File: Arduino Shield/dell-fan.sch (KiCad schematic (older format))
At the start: 50 parts, among them J1 Power, P1 Digital, P10 CONN_01X01, P11 CONN_01X01, P13 CONN_01X01, P2 Power, P3 Analog, P4 Analog, P5 PWM, P6 PWM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

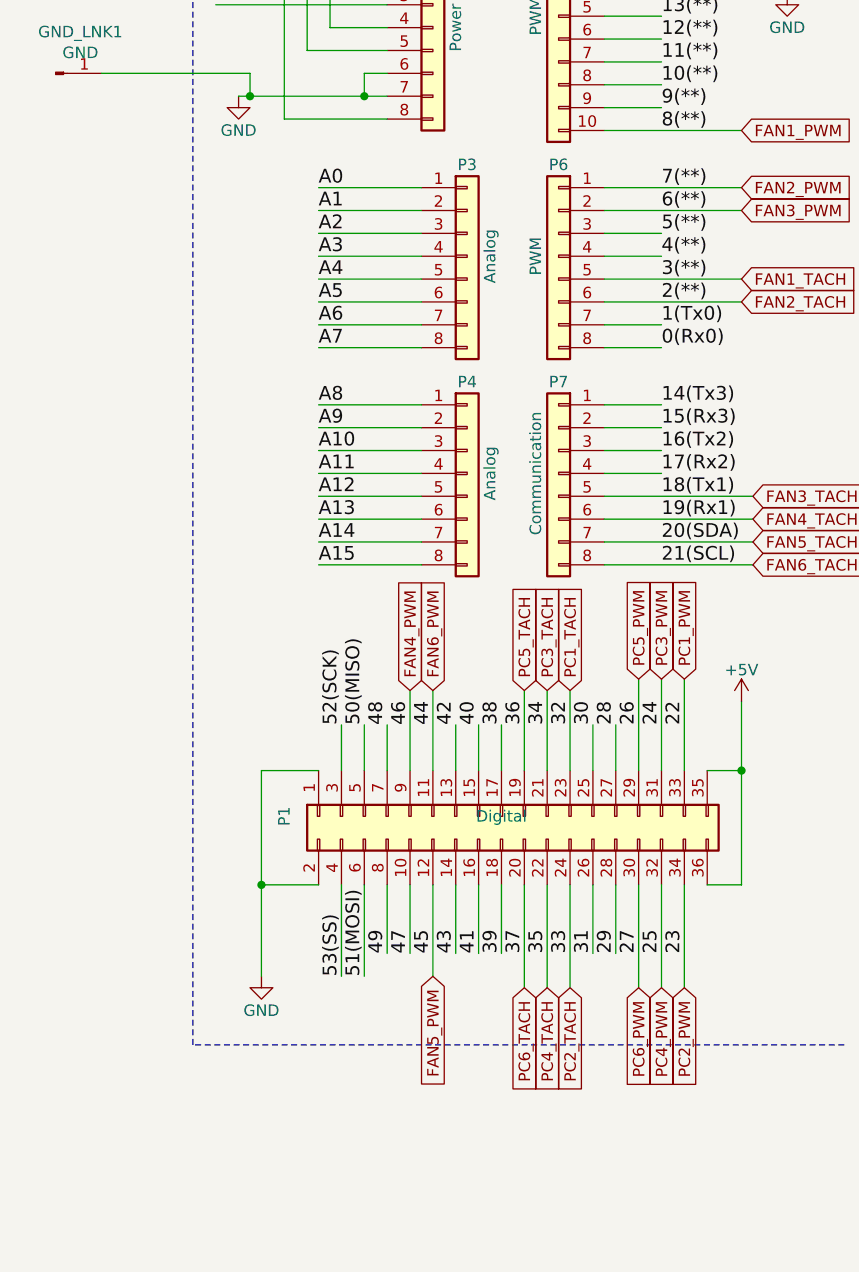
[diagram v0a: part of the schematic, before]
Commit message: moved PC Tach and PWM to D554-d69
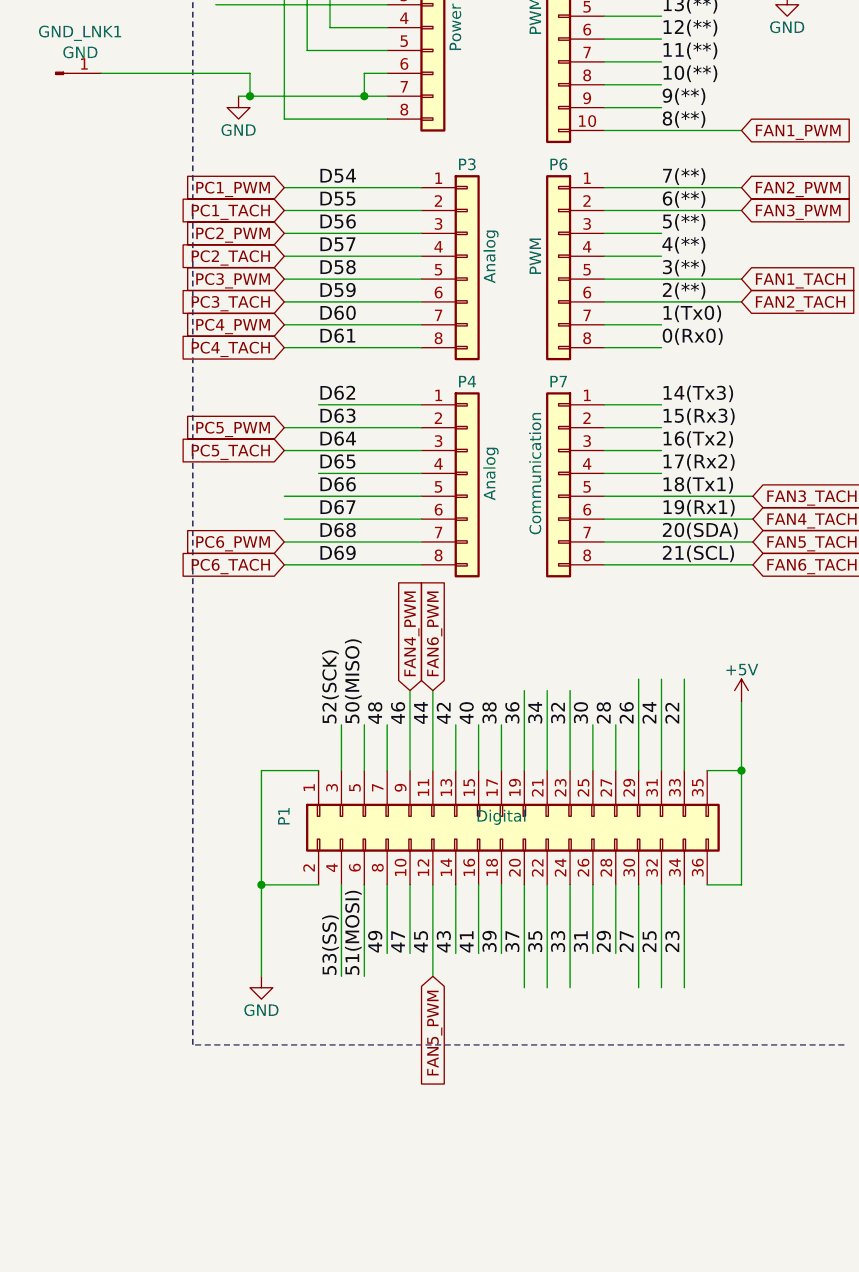
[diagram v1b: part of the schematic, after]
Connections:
- net labels added: D54, D55, D56, D57, D58, D59, D60, D61, D62, D63, D64, D65, D66, D67, D68, D69
- net labels removed: A0, A1, A10, A11, A12, A13, A14, A15, A2, A3, A4, A5, A6, A7, A8, A9
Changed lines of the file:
@@
 Vin
 Text Label 8900 2300 0    60   ~ 0
-A0
+D54
 Text Label 8900 2400 0    60   ~ 0
-A1
+D55
 Text Label 8900 2500 0    60   ~ 0
-A2
+D56
 Text Label 8900 2600 0    60   ~ 0
-A3
+D57
 Text Label 8900 2700 0    60   ~ 0
-A4
+D58
 Text Label 8900 2900 0    60   ~ 0
-A6
+D60
 Text Label 8900 3000 0    60   ~ 0
-A7
+D61
 Text Label 8900 3250 0    60   ~ 0
-A8
+D62
 Text Label 8900 3350 0    60   ~ 0
-A9
+D63
 Text Label 8900 3450 0    60   ~ 0
-A10
+D64
 Text Label 8900 3550 0    60   ~ 0
-A11
+D65
 Text Label 8900 3650 0    60   ~ 0
-A12
+D66
 Text Label 8900 3750 0    60   ~ 0
-A13
+D67
 Text Label 8900 3850 0    60   ~ 0
-A14
+D68
 Text Label 8900 3950 0    60   ~ 0
-A15
+D69
 Text Label 10500 4650 1    60   ~ 0
 22
@@
 	9350 3250 8900 3250
 Wire Wire Line
-	8900 3350 9350 3350
-Wire Wire Line
-	9350 3450 8900 3450
-Wire Wire Line
 	8900 3550 9350 3550
-Wire Wire Line
-	9350 3650 8900 3650
-Wire Wire Line
-	8900 3750 9350 3750
-Wire Wire Line
-	9350 3850 8900 3850
-Wire Wire Line
-	8900 3950 9350 3950
 Wire Wire Line
 	10400 3250 10150 3250
@@
 	1900 4550 1900 5000
 Connection ~ 1900 5000
-Wire Wire Line
-	8900 3000 9350 3000
-Wire Wire Line
-	9350 2900 8900 2900
-Wire Wire Line
-	9350 2700 8900 2700
-Wire Wire Line
-	8900 2600 9350 2600
-Wire Wire Line
-	9350 2500 8900 2500
-Wire Wire Line
-	8900 2400 9350 2400
-Wire Wire Line
-	9350 2300 8900 2300
 $Comp
 L Connector_Generic:Conn_01x08 P3
@@
 $EndComp
 Text Label 8900 2800 0    60   ~ 0
-A5
-Wire Wire Line
-	8900 2800 9350 2800
+D59
 $Comp
 L Connector_Generic:Conn_01x08 P6
@@
 Text GLabel 1100 1200 0    50   Input ~ 0
 FAN1_12v
-Text GLabel 10500 4450 1    50   Input ~ 0
+Text GLabel 8750 2300 0    50   Input ~ 0
 PC1_PWM
 Text GLabel 1100 700  0    50   Input ~ 0
@@
 Text Label 6050 3800 0    50   ~ 0
 NC
-Text GLabel 10400 4450 1    50   Input ~ 0
+Text GLabel 8750 2700 0    50   Input ~ 0
 PC3_PWM
-Text GLabel 10300 4450 1    50   Input ~ 0
+Text GLabel 8750 3350 0    50   Input ~ 0
 PC5_PWM
-Text GLabel 10000 4500 1    50   Input ~ 0
+Text GLabel 8750 2400 0    50   Input ~ 0
 PC1_TACH
-Text GLabel 10000 5800 3    50   Input ~ 0
+Text GLabel 8750 2600 0    50   Input ~ 0
 PC2_TACH
-Text GLabel 9900 4500 1    50   Input ~ 0
+Text GLabel 8750 2800 0    50   Input ~ 0
 PC3_TACH
-Text GLabel 9900 5800 3    50   Input ~ 0
+Text GLabel 8750 3000 0    50   Input ~ 0
 PC4_TACH
-Text GLabel 9800 4500 1    50   Input ~ 0
+Text GLabel 8750 3450 0    50   Input ~ 0
 PC5_TACH
-Text GLabel 9800 5800 3    50   Input ~ 0
+Text GLabel 8750 3950 0    50   Input ~ 0
 PC6_TACH
 Text GLabel 10750 2700 2    50   Input ~ 0
@@
 Text GLabel 9400 5750 3    50   Input ~ 0
 FAN5_PWM
-Text GLabel 9400 4500 1    50   Input ~ 0
-FAN6_PWM
-Text GLabel 10750 2050 2    50   Input ~ 0
-FAN1_PWM
 $Comp
 L Device:R_US R9
@@
 Wire Wire Line
 	10500 4450 10500 4850
-Text GLabel 10300 5800 3    50   Input ~ 0
+Text GLabel 8750 3850 0    50   Input ~ 0
 PC6_PWM
-Text GLabel 10400 5800 3    50   Input ~ 0
+Text GLabel 8750 2900 0    50   Input ~ 0
 PC4_PWM
-Text GLabel 10500 5800 3    50   Input ~ 0
+Text GLabel 8750 2500 0    50   Input ~ 0
 PC2_PWM
 Wire Wire Line
@@
 Text Notes 1750 5750 0    50   ~ 0
 NC
+Text GLabel 10750 2050 2    50   Input ~ 0
+FAN1_PWM
+Wire Wire Line
+	8750 2300 9350 2300
+Wire Wire Line
+	8750 2400 9350 2400
+Wire Wire Line
+	8750 2600 9350 2600
+Wire Wire Line
+	8750 2500 9350 2500
+Wire Wire Line
+	8750 2700 9350 2700
+Wire Wire Line
+	8750 2800 9350 2800
+Wire Wire Line
+	8750 3000 9350 3000
+Wire Wire Line
+	8750 2900 9350 2900
+Text GLabel 9400 4500 1    50   Input ~ 0
+FAN6_PWM
+Wire Wire Line
+	8750 3950 9350 3950
+Wire Wire Line
+	8750 3850 9350 3850
+Wire Wire Line
+	8750 3750 9350 3750
+Wire Wire Line
+	8750 3350 9350 3350
+Wire Wire Line
+	8750 3450 9350 3450
+Wire Wire Line
+	8750 3650 9350 3650
 $EndSCHEMATC

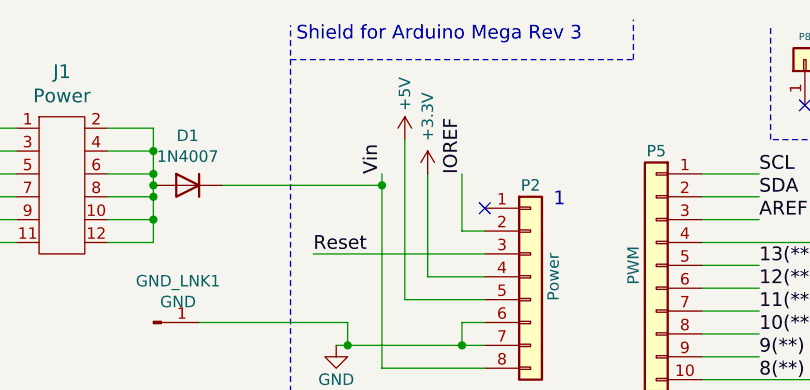
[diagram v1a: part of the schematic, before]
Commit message: fixed ground plane issue
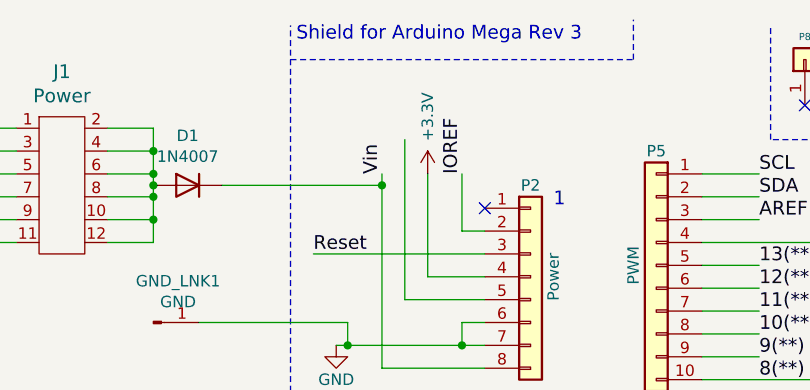
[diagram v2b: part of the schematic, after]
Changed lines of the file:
@@
 Reset
-$Comp
-L power:+5V #PWR02
-U 1 1 56D71D10
-P 8850 1000
-F 0 "#PWR02" H 8850 850 50  0001 C CNN
-F 1 "+5V" V 8850 1200 50  0000 C CNN
-F 2 "" H 8850 1000 50  0000 C CNN
-F 3 "" H 8850 1000 50  0000 C CNN
-	1    8850 1000
-	1    0    0    -1
-$EndComp
 $Comp
 L power:GND #PWR03

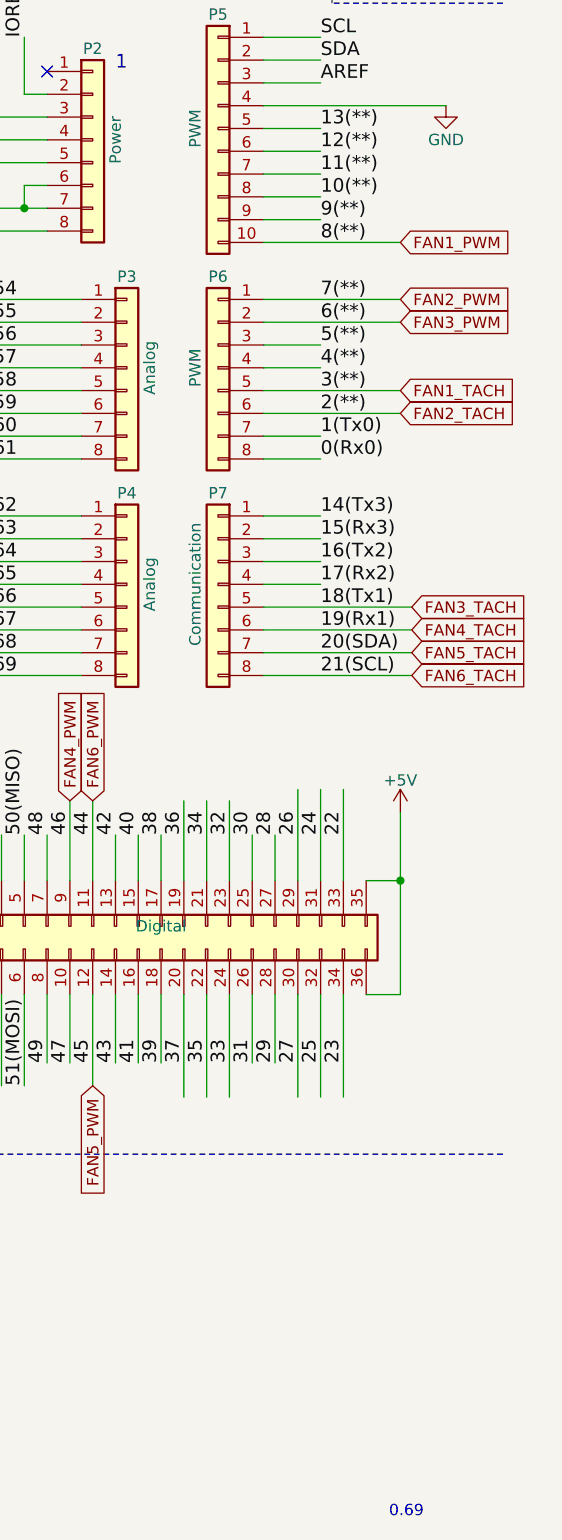
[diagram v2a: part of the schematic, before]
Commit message: No interrupts means better pin placement
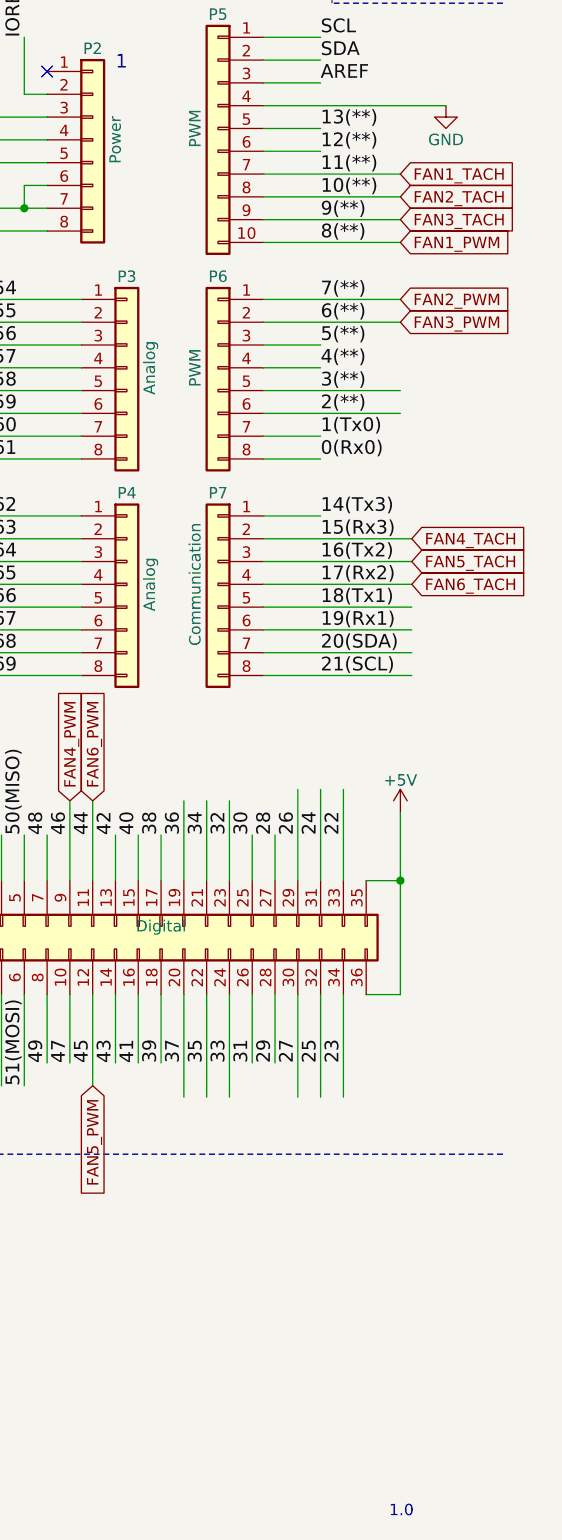
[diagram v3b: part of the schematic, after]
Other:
- note added: "1.0"
- note removed: "0.69"
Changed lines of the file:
@@
 	10400 1650 10150 1650
 Wire Wire Line
-	10150 1750 10400 1750
-Wire Wire Line
-	10150 1850 10400 1850
-Wire Wire Line
-	10400 1950 10150 1950
-Wire Wire Line
 	10400 2500 10150 2500
 Wire Wire Line
@@
 Wire Wire Line
 	10400 3250 10150 3250
-Wire Wire Line
-	10150 3350 10400 3350
-Wire Wire Line
-	10400 3450 10150 3450
-Wire Wire Line
-	10150 3550 10400 3550
 Wire Wire Line
 	10200 4850 10200 4650
@@
 Text GLabel 8750 3950 0    50   Input ~ 0
 PC6_TACH
-Text GLabel 10750 2700 2    50   Input ~ 0
+Text GLabel 10750 1750 2    50   Input ~ 0
 FAN1_TACH
-Text GLabel 10750 2800 2    50   Input ~ 0
+Text GLabel 10750 1850 2    50   Input ~ 0
 FAN2_TACH
-Text GLabel 10800 3650 2    50   Input ~ 0
+Text GLabel 10750 1950 2    50   Input ~ 0
 FAN3_TACH
-Text GLabel 10800 3750 2    50   Input ~ 0
+Text GLabel 10800 3350 2    50   Input ~ 0
 FAN4_TACH
-Text GLabel 10800 3850 2    50   Input ~ 0
+Text GLabel 10800 3450 2    50   Input ~ 0
 FAN5_TACH
-Text GLabel 10800 3950 2    50   Input ~ 0
+Text GLabel 10800 3550 2    50   Input ~ 0
 FAN6_TACH
 Text GLabel 10750 2300 2    50   Input ~ 0
@@
 	2800 3600 2950 3600
 Text Notes 10700 7650 0    50   ~ 0
-0.69
+1.0
 Wire Wire Line
 	10500 4450 10500 4850
@@
 Wire Wire Line
 	8750 3650 9350 3650
+Wire Wire Line
+	10150 3350 10800 3350
+Wire Wire Line
+	10150 3450 10800 3450
+Wire Wire Line
+	10150 3550 10800 3550
+Wire Wire Line
+	10150 1750 10750 1750
+Wire Wire Line
+	10150 1850 10750 1850
+Wire Wire Line
+	10150 1950 10750 1950
 $EndSCHEMATC

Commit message: removing ground link as the board uses a common ground
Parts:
- removed GND_LNK1: GND, Connector_PinHeader_2.54mm:PinHeader_1x01_P2.54mm_Vertical, symbol Connector:Conn_01x01_Male
- J1: symbol dk_Rectangular-Connectors-Headers-Male-Pins:67996-412HLF -> dell-fan-rescue:67996-412HLF-dk_Rectangular-Connectors-Headers-Male-Pins
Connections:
- wire segments 244 -> 241
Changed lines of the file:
@@
 	9100 1800 9100 1900
-Wire Wire Line
-	9100 1900 8600 1900
 Wire Wire Line
 	9200 1900 9100 1900
@@
 	10150 3950 10800 3950
 $Comp
-L dk_Rectangular-Connectors-Headers-Male-Pins:67996-412HLF J1
+L dell-fan-rescue:67996-412HLF-dk_Rectangular-Connectors-Headers-Male-Pins J1
 U 1 1 624413EB
 P 7350 1150
@@
 Text Notes 5300 4750 0    50   ~ 0
 Loopback
-$Comp
-L Connector:Conn_01x01_Male GND_LNK1
-U 1 1 617EF8EC
-P 7750 1800
-F 0 "GND_LNK1" H 7858 1981 50  0000 C CNN
-F 1 "GND" H 7858 1890 50  0000 C CNN
-F 2 "Connector_PinHeader_2.54mm:PinHeader_1x01_P2.54mm_Vertical" H 7750 1800 50  0001 C CNN
-F 3 "~" H 7750 1800 50  0001 C CNN
-	1    7750 1800
-	1    0    0    -1
-$EndComp
-Wire Wire Line
-	8600 1900 8600 1800
-Wire Wire Line
-	8600 1800 7950 1800
-Connection ~ 8600 1900
-Wire Wire Line
-	8600 1900 8550 1900
 Text GLabel 1900 4550 2    50   Input ~ 0
 FAN1_TACH_IN
@@
 Wire Wire Line
 	10150 1950 10750 1950
+Wire Wire Line
+	8550 1900 9100 1900
 $EndSCHEMATC

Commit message: updating resistor size in schematic
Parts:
- R1, R10, R11, R12, R2, R3, R4, R5, R6, R7, R8, R9: footprint Resistor_THT:R_Box_L8.4mm_W2.5mm_P5.08mm -> Resistor_THT:R_Box_L13.0mm_W4.0mm_P9.00mm
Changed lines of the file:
@@
 F 0 "R1" H 1968 5196 50  0000 L CNN
 F 1 "10k" H 1968 5105 50  0000 L CNN
-F 2 "Resistor_THT:R_Box_L8.4mm_W2.5mm_P5.08mm" V 1940 5140 50  0001 C CNN
+F 2 "Resistor_THT:R_Box_L13.0mm_W4.0mm_P9.00mm" V 1940 5140 50  0001 C CNN
 F 3 "~" H 1900 5150 50  0001 C CNN
 	1    1900 5150
@@
 F 0 "R2" V 1545 5000 50  0000 C CNN
 F 1 "220k" V 1636 5000 50  0000 C CNN
-F 2 "Resistor_THT:R_Box_L8.4mm_W2.5mm_P5.08mm" V 1790 4990 50  0001 C CNN
+F 2 "Resistor_THT:R_Box_L13.0mm_W4.0mm_P9.00mm" V 1790 4990 50  0001 C CNN
 F 3 "~" H 1750 5000 50  0001 C CNN
 	1    1750 5000
@@
 F 0 "R3" H 3418 5196 50  0000 L CNN
 F 1 "10k" H 3418 5105 50  0000 L CNN
-F 2 "Resistor_THT:R_Box_L8.4mm_W2.5mm_P5.08mm" V 3390 5140 50  0001 C CNN
+F 2 "Resistor_THT:R_Box_L13.0mm_W4.0mm_P9.00mm" V 3390 5140 50  0001 C CNN
 F 3 "~" H 3350 5150 50  0001 C CNN
 	1    3350 5150
@@
 F 0 "R4" V 2995 5000 50  0000 C CNN
 F 1 "220k" V 3086 5000 50  0000 C CNN
-F 2 "Resistor_THT:R_Box_L8.4mm_W2.5mm_P5.08mm" V 3240 4990 50  0001 C CNN
+F 2 "Resistor_THT:R_Box_L13.0mm_W4.0mm_P9.00mm" V 3240 4990 50  0001 C CNN
 F 3 "~" H 3200 5000 50  0001 C CNN
 	1    3200 5000
@@
 F 0 "R5" H 4768 5196 50  0000 L CNN
 F 1 "10k" H 4768 5105 50  0000 L CNN
-F 2 "Resistor_THT:R_Box_L8.4mm_W2.5mm_P5.08mm" V 4740 5140 50  0001 C CNN
+F 2 "Resistor_THT:R_Box_L13.0mm_W4.0mm_P9.00mm" V 4740 5140 50  0001 C CNN
 F 3 "~" H 4700 5150 50  0001 C CNN
 	1    4700 5150
@@
 F 0 "R6" V 4345 5000 50  0000 C CNN
 F 1 "220k" V 4436 5000 50  0000 C CNN
-F 2 "Resistor_THT:R_Box_L8.4mm_W2.5mm_P5.08mm" V 4590 4990 50  0001 C CNN
+F 2 "Resistor_THT:R_Box_L13.0mm_W4.0mm_P9.00mm" V 4590 4990 50  0001 C CNN
 F 3 "~" H 4550 5000 50  0001 C CNN
 	1    4550 5000
@@
 F 0 "R7" H 6218 5196 50  0000 L CNN
 F 1 "10k" H 6218 5105 50  0000 L CNN
-F 2 "Resistor_THT:R_Box_L8.4mm_W2.5mm_P5.08mm" V 6190 5140 50  0001 C CNN
+F 2 "Resistor_THT:R_Box_L13.0mm_W4.0mm_P9.00mm" V 6190 5140 50  0001 C CNN
 F 3 "~" H 6150 5150 50  0001 C CNN
 	1    6150 5150
@@
 F 0 "R8" V 5795 5000 50  0000 C CNN
 F 1 "220k" V 5886 5000 50  0000 C CNN
-F 2 "Resistor_THT:R_Box_L8.4mm_W2.5mm_P5.08mm" V 6040 4990 50  0001 C CNN
+F 2 "Resistor_THT:R_Box_L13.0mm_W4.0mm_P9.00mm" V 6040 4990 50  0001 C CNN
 F 3 "~" H 6000 5000 50  0001 C CNN
 	1    6000 5000
@@
 F 0 "R9" H 1868 7146 50  0000 L CNN
 F 1 "10k" H 1868 7055 50  0000 L CNN
-F 2 "Resistor_THT:R_Box_L8.4mm_W2.5mm_P5.08mm" V 1840 7090 50  0001 C CNN
+F 2 "Resistor_THT:R_Box_L13.0mm_W4.0mm_P9.00mm" V 1840 7090 50  0001 C CNN
 F 3 "~" H 1800 7100 50  0001 C CNN
 	1    1800 7100
@@
 F 0 "R10" V 1445 6950 50  0000 C CNN
 F 1 "220k" V 1536 6950 50  0000 C CNN
-F 2 "Resistor_THT:R_Box_L8.4mm_W2.5mm_P5.08mm" V 1690 6940 50  0001 C CNN
+F 2 "Resistor_THT:R_Box_L13.0mm_W4.0mm_P9.00mm" V 1690 6940 50  0001 C CNN
 F 3 "~" H 1650 6950 50  0001 C CNN
 	1    1650 6950
@@
 F 0 "R11" H 3318 7146 50  0000 L CNN
 F 1 "10k" H 3318 7055 50  0000 L CNN
-F 2 "Resistor_THT:R_Box_L8.4mm_W2.5mm_P5.08mm" V 3290 7090 50  0001 C CNN
+F 2 "Resistor_THT:R_Box_L13.0mm_W4.0mm_P9.00mm" V 3290 7090 50  0001 C CNN
 F 3 "~" H 3250 7100 50  0001 C CNN
 	1    3250 7100
@@
 F 0 "R12" V 2895 6950 50  0000 C CNN
 F 1 "220k" V 2986 6950 50  0000 C CNN
-F 2 "Resistor_THT:R_Box_L8.4mm_W2.5mm_P5.08mm" V 3140 6940 50  0001 C CNN
+F 2 "Resistor_THT:R_Box_L13.0mm_W4.0mm_P9.00mm" V 3140 6940 50  0001 C CNN
 F 3 "~" H 3100 6950 50  0001 C CNN
 	1    3100 6950
